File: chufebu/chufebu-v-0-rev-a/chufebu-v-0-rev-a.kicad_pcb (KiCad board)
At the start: 2 copper layers, 200 x 50 mm, 22 parts, among them J1 Conn_02x08_Odd_Even, J2 Conn_02x08_Odd_Even, J3 Conn_02x08_Odd_Even, J4 Conn_02x08_Odd_Even, J5 Conn_02x08_Odd_Even, J6 Barrel_Jack_Switch, Q1 AO3401A, U1 URA2412YMD-20WR3_C5369773, U2 L7805

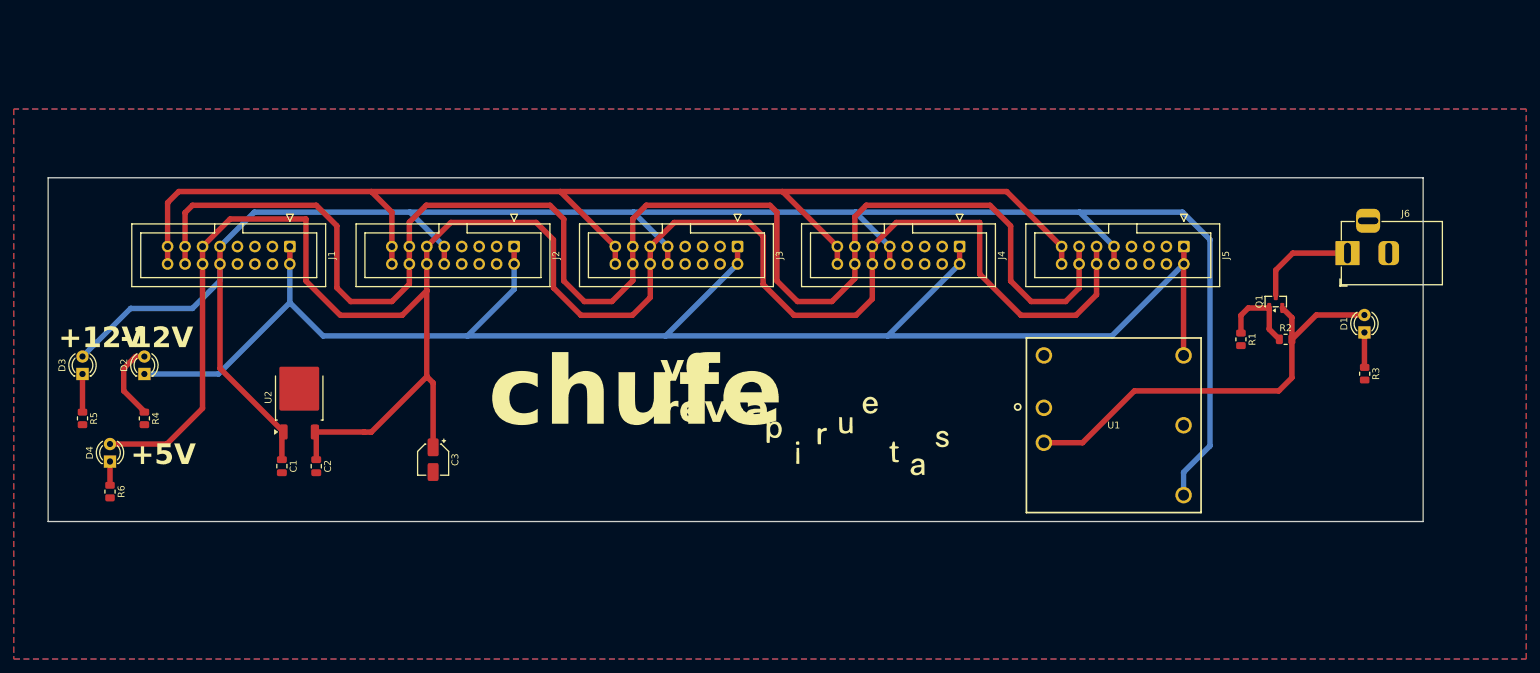
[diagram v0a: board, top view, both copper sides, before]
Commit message: agregar borrador pcb chufe
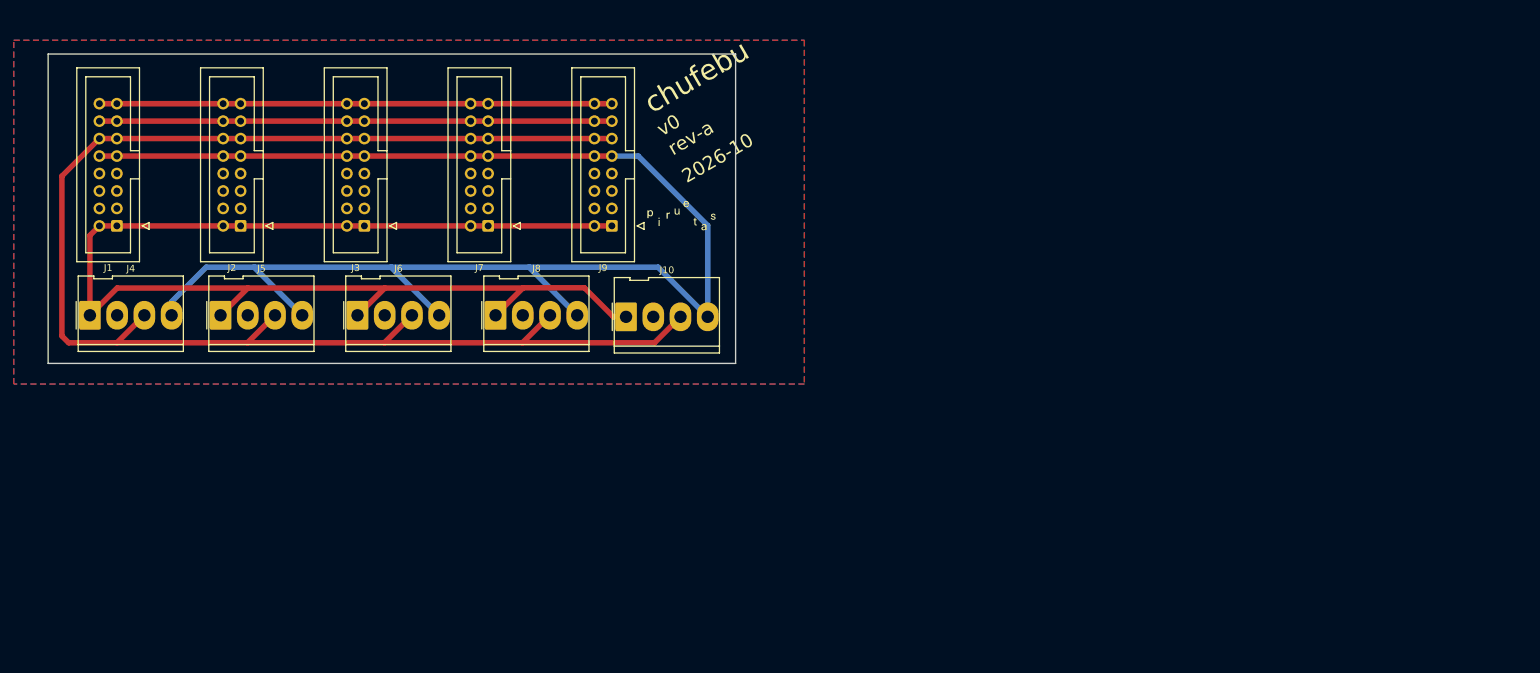
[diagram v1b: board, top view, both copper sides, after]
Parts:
- removed C1, C2: 100n, Capacitor_SMD:C_0805_2012Metric
- removed C3: 22u, Capacitor_SMD:CP_Elec_4x5.4
- removed D1, D2, D3, D4: LED, LED_THT:LED_D3.0mm
- removed Q1: AO3401A, Package_TO_SOT_SMD:SOT-23
- removed R1, R6: 2k2, Resistor_SMD:R_0805_2012Metric
- removed R2: 1k, Resistor_SMD:R_0805_2012Metric
- removed R3, R4, R5: 10k, Resistor_SMD:R_0805_2012Metric
- removed U1: URA2412YMD-20WR3_C5369773, easyeda2kicad:PWRM-TH_YLPTEC_VRBXXXXYMD-20WR3
- removed U2: L7805, Package_TO_SOT_SMD:TO-252-2
- added J10: Conn_01x04_Pin, Connector_Molex:Molex_KK-396_5273-04A_1x04_P3.96mm_Vertical, F.Cu at (109.1, 60.2)
- added J7: Conn_02x08_Odd_Even, Connector_IDC:IDC-Header_2x08_P2.54mm_Vertical, F.Cu at (89.0, 47.0)
- added J8: Conn_01x04_Pin, Connector_Molex:Molex_KK-396_5273-04A_1x04_P3.96mm_Vertical, F.Cu at (90.1, 60.0)
- added J9: Conn_02x08_Odd_Even, Connector_IDC:IDC-Header_2x08_P2.54mm_Vertical, F.Cu at (107.0, 47.0)
- J4, J5: value Conn_02x08_Odd_Even -> Conn_01x04_Pin; footprint Connector_IDC:IDC-Header_2x08_P2.54mm_Vertical -> Connector_Molex:Molex_KK-396_5273-04A_1x04_P3.96mm_Vertical
- J6: value Barrel_Jack_Switch -> Conn_01x04_Pin; footprint Connector_BarrelJack:BarrelJack_Horizontal -> Connector_Molex:Molex_KK-396_5273-04A_1x04_P3.96mm_Vertical
- moved J6 144.3 mm to (70.0, 60.0), turned to 0 degrees
- moved J5 140.5 mm to (50.1, 60.0), turned to 0 degrees
- moved J4 126.9 mm to (31.1, 60.0), turned to 0 degrees
- moved J3 54.4 mm to (71.0, 47.0), turned to 180 degrees
- moved J2 39.9 mm to (53.0, 47.0), turned to 180 degrees
- moved J1 25.3 mm to (35.0, 47.0), turned to 180 degrees
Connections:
- J4 pad 2: -12V -> GND
- J4 pad 3: GND -> +5V
- J4 pad 4: GND -> +12V
- J5 pad 2: -12V -> GND
- J5 pad 3: GND -> +5V
- J5 pad 4: GND -> +12V
- J6 pad 1: Net-(Q1-D) -> -12V
- J6 pad 3: GND -> +5V
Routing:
- net /CV: track 222.3 -> 74.5 mm
- net /GATE: track 185.0 -> 74.5 mm
- net +5V: track 295.8 -> 220.1 mm
- net +12V: track 286.9 -> 220.7 mm
- net Net-(D1-A): track 62.7 -> 0.00 mm
- net -12V: track 236.3 -> 186.3 mm
- net Net-(Q1-D): track 15.1 -> 0.00 mm
- net Net-(Q1-G): track 12.3 -> 0.00 mm
- net Net-(D2-A): track 11.3 -> 0.00 mm
- net Net-(D3-K): track 5.55 -> 0.00 mm
- net Net-(D1-K): track 5.10 -> 0.00 mm
- net Net-(D4-K): track 3.46 -> 0.00 mm
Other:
- board size 200 x 50 mm -> 100 x 45 mm
- board text added: "2026-10"
- board text added: "chufebu"
- board text added: "v0 rev-a"
- board text removed: "+12V"
- board text removed: "+5V"
- board text removed: "-12V"
- board text removed: "chufe"
- board text removed: "rev-a"
- board text removed: "v0"

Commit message: agregar chufebu
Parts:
- added H1: M3, MountingHole:MountingHole_3.2mm_M3, F.Cu at (120.0, 27.0)
- added H2: M3, MountingHole:MountingHole_3.2mm_M3, F.Cu at (29.0, 62.0)
- J8: value Conn_01x04_Pin -> Conn_02x08_Odd_Even; footprint Connector_Molex:Molex_KK-396_5273-04A_1x04_P3.96mm_Vertical -> Connector_IDC:IDC-Header_2x08_P2.54mm_Vertical
- J9: value Conn_02x08_Odd_Even -> Conn_01x04_Pin; footprint Connector_IDC:IDC-Header_2x08_P2.54mm_Vertical -> Connector_Molex:Molex_KK-396_5273-04A_1x04_P3.96mm_Vertical
- moved J9 21.4 mm to (90.0, 60.0), turned to 0 degrees
- moved J8 21.3 mm to (107.0, 47.0), turned to 180 degrees
- moved J4 4.92 mm to (36.0, 60.0)
- moved J5 3.92 mm to (54.0, 60.0)
- moved J6 2.00 mm to (72.0, 60.0)
- moved J10 1.08 mm to (108.0, 60.0)
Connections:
- J8 pad 2: GND -> -12V
- J8 pad 3: +5V -> GND
- J8 pad 4: +12V -> GND
- J9 pad 2: -12V -> GND
- J9 pad 3: GND -> +5V
- J9 pad 4: GND -> +12V
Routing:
- net +5V: track 220.1 -> 196.2 mm
- net +12V: track 220.7 -> 203.3 mm
- net -12V: track 186.3 -> 181.4 mm
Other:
- board text added: "v0.1 rev-a"
- board text removed: "v0 rev-a"

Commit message: revisado drc
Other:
- board text added: "-12 gnd 5 12"
- board text added: "gate cv 5 12 gnd gnd gnd -12"
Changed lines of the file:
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@@
 			(at 5.94 -6.8 0)
 			(layer "F.SilkS")
+			(hide yes)
 			(effects
 				(font
@@
 			(at 0 -4.15 0)
 			(layer "F.SilkS")
+			(hide yes)
 			(effects
 				(font
@@
 			(at 1.27 -6.1 0)
 			(layer "F.SilkS")
+			(hide yes)
 			(effects
 				(font
@@
 			(at 5.94 -6.8 0)
 			(layer "F.SilkS")
+			(hide yes)
 			(effects
 				(font
@@
 			(at 1.27 -6.1 0)
 			(layer "F.SilkS")
+			(hide yes)
 			(effects
 				(font
@@
 			(at 5.94 -6.8 0)
 			(layer "F.SilkS")
+			(hide yes)
 			(effects
 				(font
@@
 			(at 1.27 -6.1 0)
 			(layer "F.SilkS")
+			(hide yes)
 			(effects
 				(font
@@
 			(at 1.27 -6.1 0)
 			(layer "F.SilkS")
+			(hide yes)
 			(effects
 				(font
@@
 			(at 5.94 -6.8 0)
 			(layer "F.SilkS")
+			(hide yes)
 			(effects
 				(font
@@
 			(at 0 -4.15 0)
 			(layer "F.SilkS")
+			(hide yes)
 			(effects
 				(font
@@
 			(at 5.94 -6.8 0)
 			(layer "F.SilkS")
+			(hide yes)
 			(effects
 				(font
@@
 			(at 1.27 -6.1 0)
 			(layer "F.SilkS")
+			(hide yes)
 			(effects
 				(font
@@
 		(layer "Edge.Cuts")
 	)
+	(gr_text "-12 gnd 5 12"
+		(at 34.85662 54.04762 0)
+		(layer "F.SilkS")
+		(effects
+			(font
+				(size 1.2 1.2)
+				(thickness 0.1625)
+			)
+			(justify left bottom)
+		)
+	)
+	(gr_text "gate\ncv\n5\n12\ngnd\ngnd\ngnd\n-12"
+		(at 39.517399 48.273649 0)
+		(layer "F.SilkS")
+		(effects
+			(font
+				(size 1.6 1.6)
+				(thickness 0.1625)
+			)
+			(justify left bottom)
+		)
+	)
 	(gr_text "\n\nv0.1 rev-a"
 		(at 114 45 30)
@@
 		(hatch edge 0.5)
 		(connect_pads
-			(clearance 0.5)
+			(clearance 0.55)
 		)
 		(min_thickness 0.25)
